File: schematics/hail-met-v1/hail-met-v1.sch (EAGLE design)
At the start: 96 parts, among them IC1 MCP73871, IC2 78L05Z, J1 AVR_SPI_PRG_6PTH, U1 ATMEGA328P, Y1 16MHZ

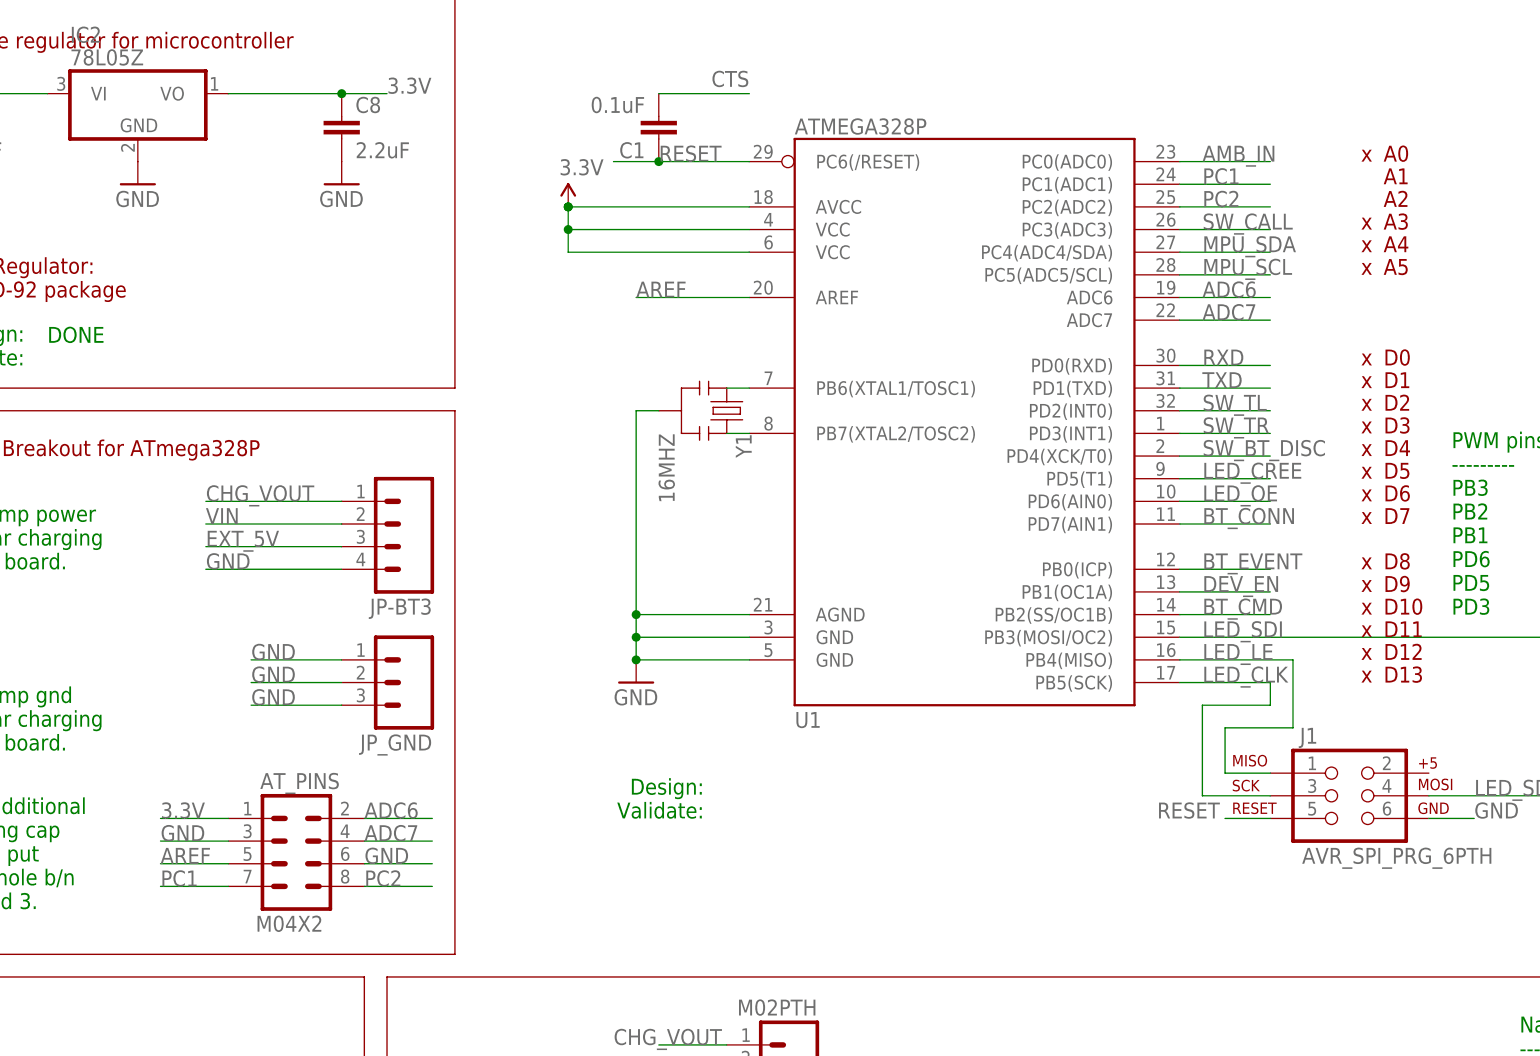
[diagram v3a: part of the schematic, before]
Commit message: modified board with audio amp values
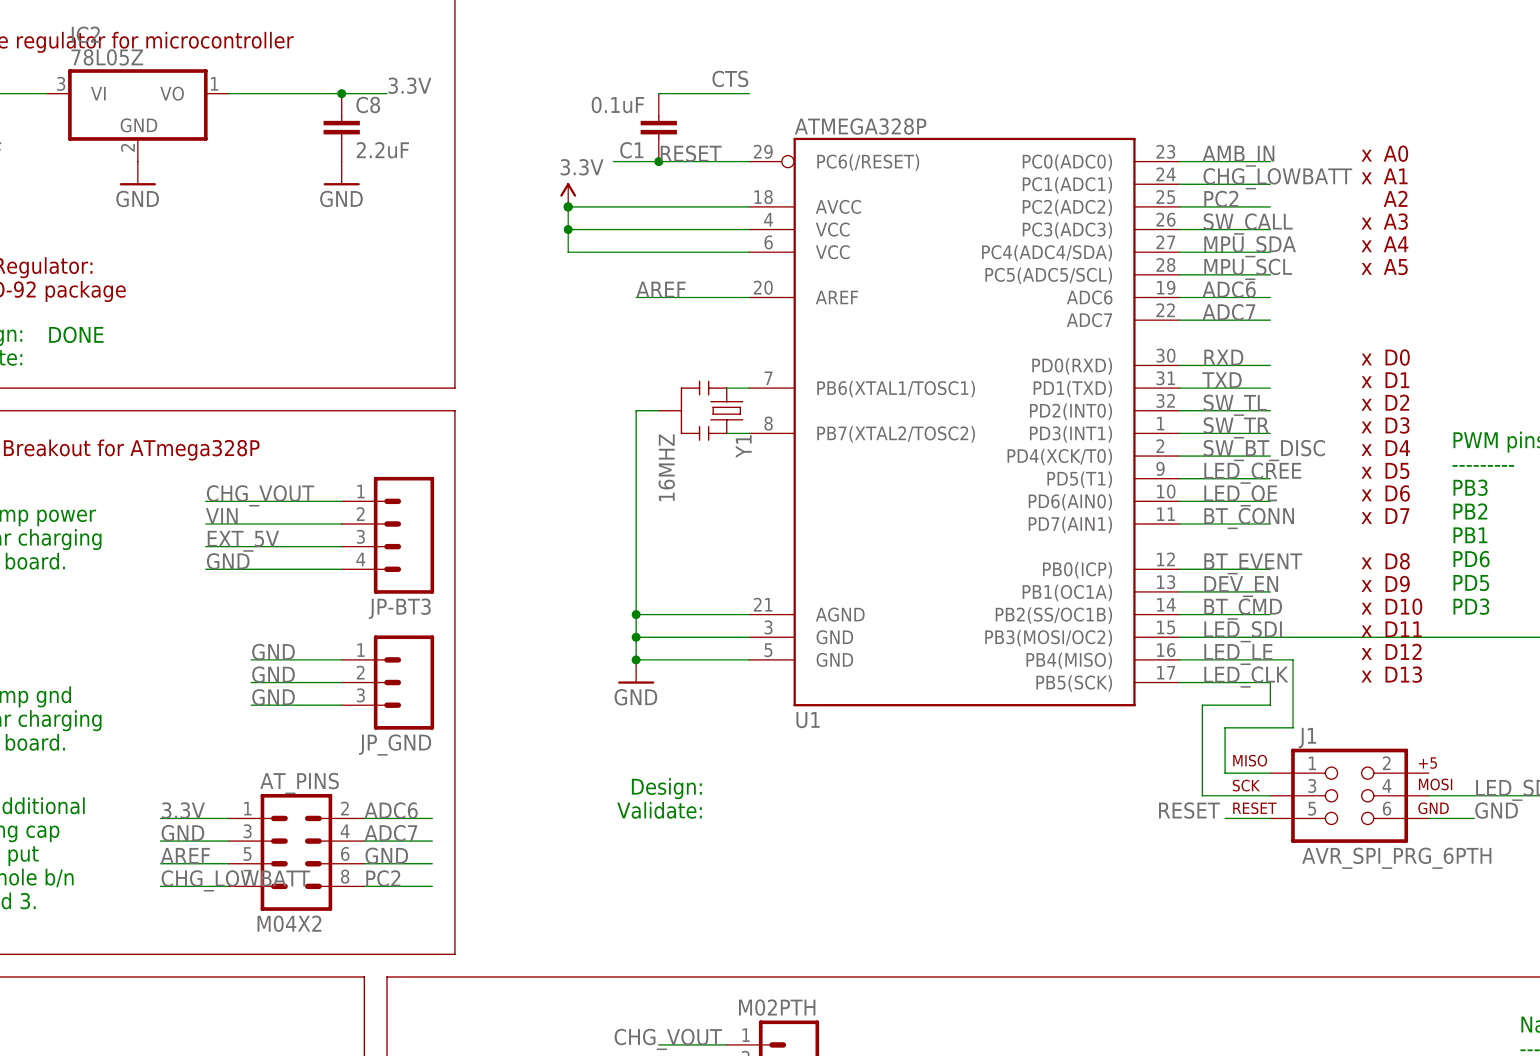
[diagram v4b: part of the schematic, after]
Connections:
- removed net PC1: AT_PINS.7, U1.PC1(ADC1)
- net CHG_LOWBATT: now also AT_PINS.7, U1.PC1(ADC1)
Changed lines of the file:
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@@
   125mA: 8.2K (our spec)
   1mA: 100K (Adafruit spec)</text>
+<text x="162.56" y="81.28" size="1.778" layer="94">x</text>
 </plain>
 <instances>
@@
 </segment>
 </net>
-<net name="PC1" class="0">
-<segment>
-<pinref part="U1" gate="G$1" pin="PC1(ADC1)"/>
-<wire x1="142.24" y1="81.28" x2="152.4" y2="81.28" width="0.1524" layer="91"/>
-<label x="144.78" y="81.28" size="1.778" layer="95"/>
-</segment>
-<segment>
-<pinref part="AT_PINS" gate="G$1" pin="7"/>
-<wire x1="27.94" y1="2.54" x2="35.56" y2="2.54" width="0.1524" layer="91"/>
-<label x="27.94" y="2.54" size="1.778" layer="95"/>
-</segment>
-</net>
 <net name="BT_VOL_UP" class="0">
 <segment>
@@
 <label x="180.34" y="-66.04" size="1.778" layer="95"/>
 </segment>
-</net>
+<segment>
+<pinref part="U1" gate="G$1" pin="PC1(ADC1)"/>
+<wire x1="142.24" y1="81.28" x2="152.4" y2="81.28" width="0.1524" layer="91"/>
+<label x="144.78" y="81.28" size="1.778" layer="95"/>
+</segment>
+<segment>
+<pinref part="AT_PINS" gate="G$1" pin="7"/>
+<wire x1="27.94" y1="2.54" x2="35.56" y2="2.54" width="0.1524" layer="91"/>
+<label x="27.94" y="2.54" size="1.778" layer="95"/>
+</segment>
+</net>
